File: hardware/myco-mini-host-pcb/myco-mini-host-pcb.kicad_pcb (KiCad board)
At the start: 2 copper layers, 190 x 115 mm, 22 parts, among them J1 Conn_01x17_Female, J2 Conn_01x17_Female, Q1 AO3401A, Q2 AO3401A, SW1 EM-04-Q, U1 XC9145B33C0R-G, U2 SHT40-AD1B-R2, U3 BH1750FVI-TR

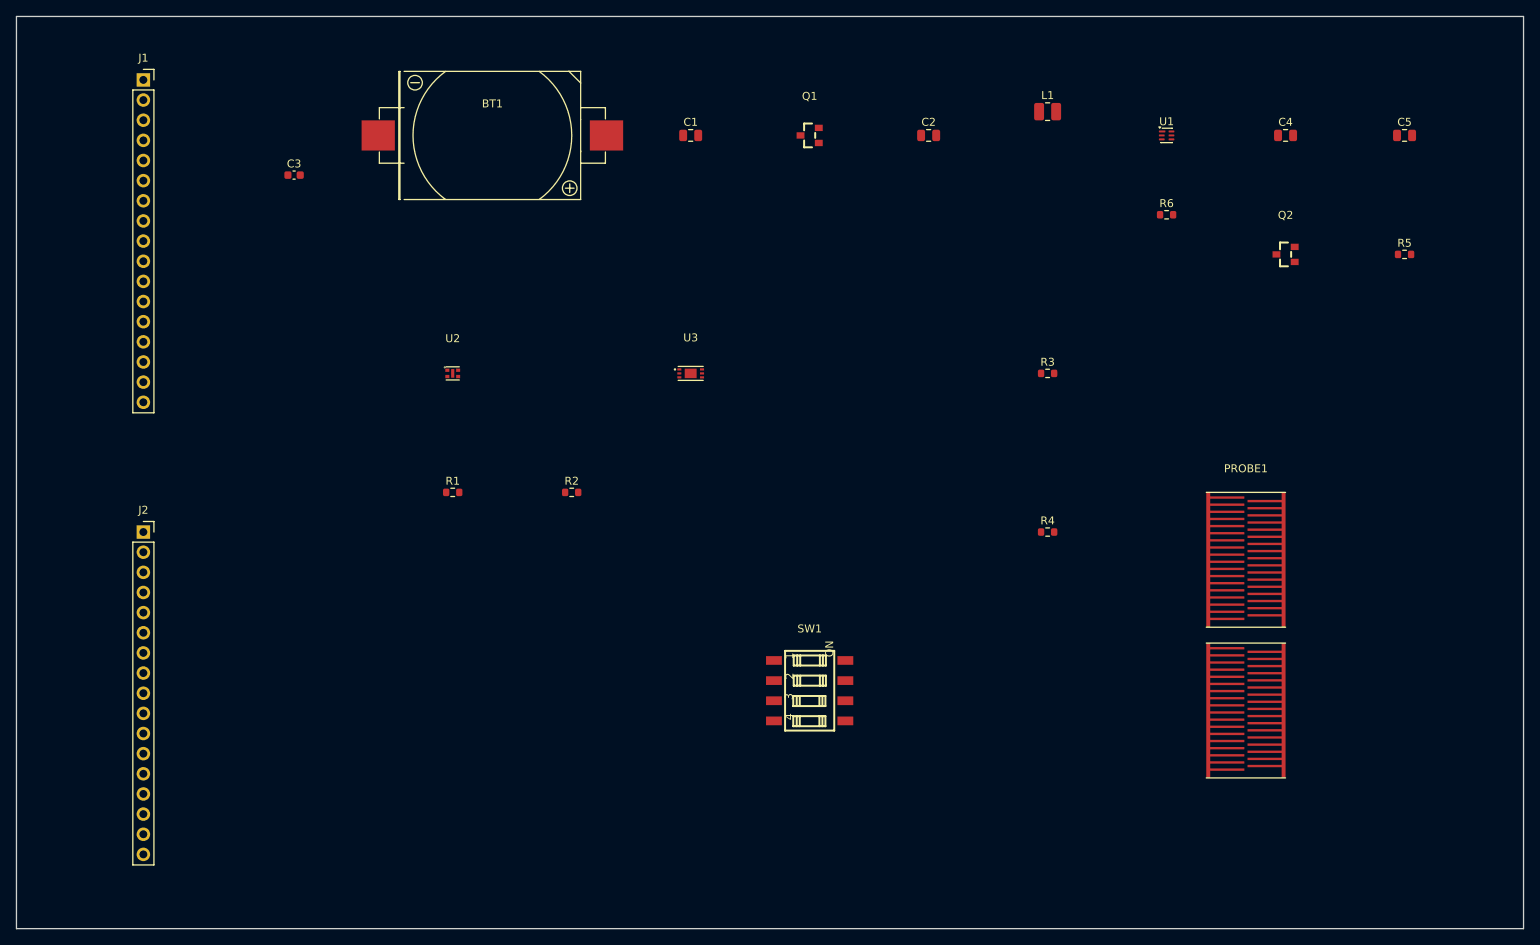
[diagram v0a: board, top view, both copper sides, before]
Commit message: fix: header rows J1/J2 en colonnes parallèles à 25.4mm (interface breakout réelle)
J1/J2 étaient empilés verticalement au lieu d'être côte à côte. Corrigé pour
matcher l'espacement centre-à-centre exact des headers J1/J4 du breakout
an54lq-15 (25.4mm, voir docs/host-pcb-design-brief.md sec.2).

Co-Authored-By: Claude Sonnet 5 <noreply@anthropic.com>
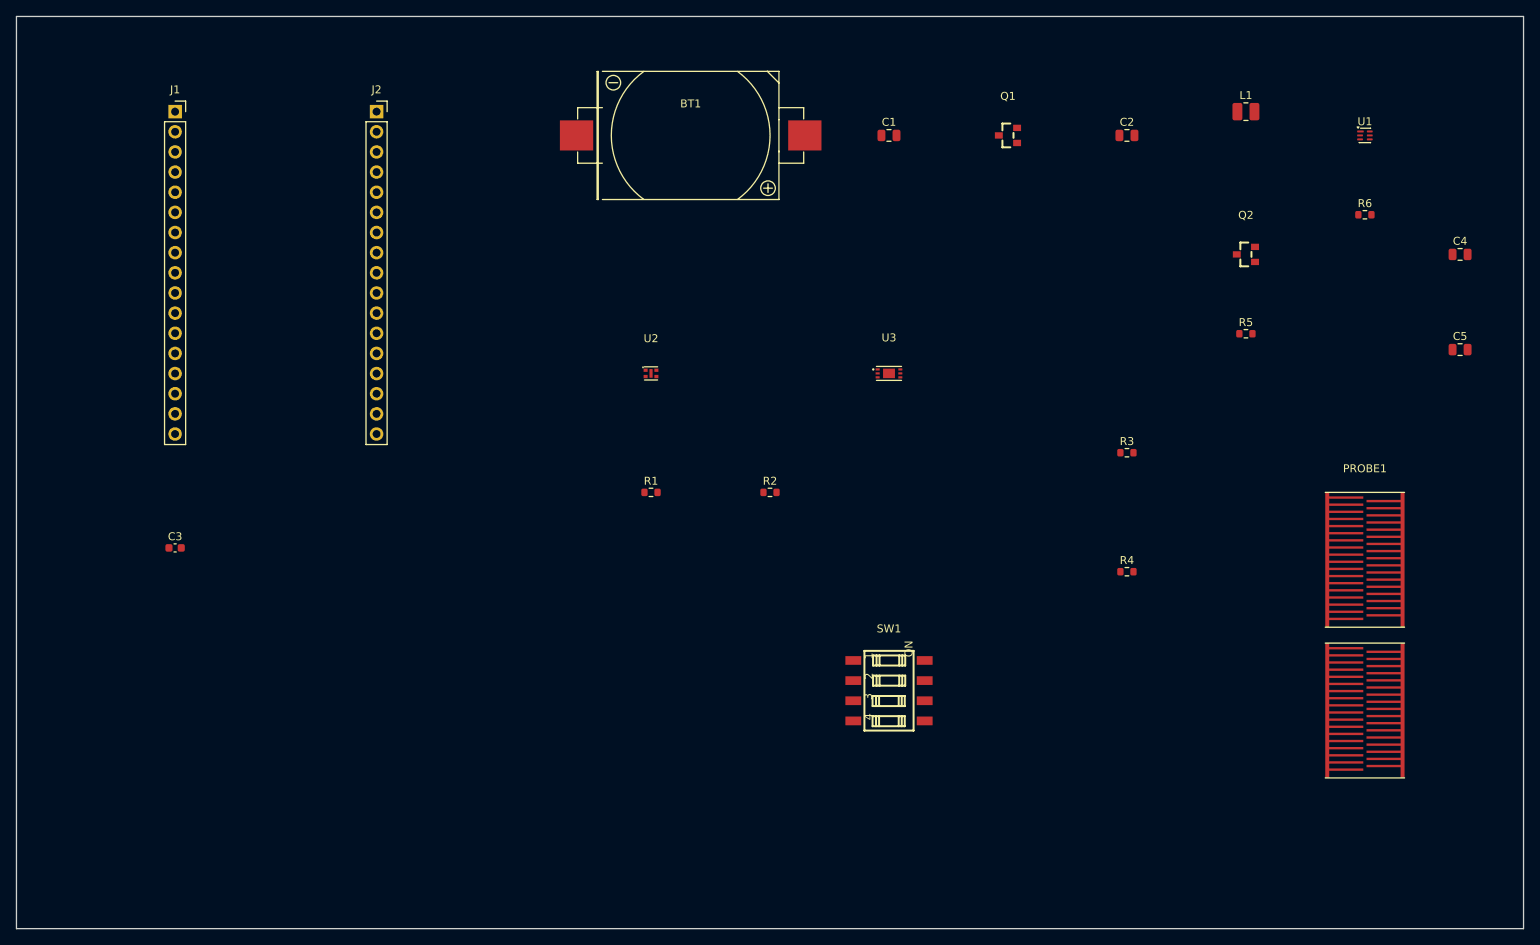
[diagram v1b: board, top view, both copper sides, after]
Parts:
- moved J2 60.6 mm to (45.4, 12.0)
- moved C3 49.3 mm to (20.0, 67.0)
- moved C5 27.9 mm to (182.0, 42.0)
- moved C4 26.6 mm to (182.0, 30.0)
- moved BT1 25.0 mm to (85.0, 15.0)
- moved C1 25.0 mm to (110.0, 15.0)
- moved C2 25.0 mm to (140.0, 15.0)
- moved L1 25.0 mm to (155.0, 12.0)
- moved Q1 25.0 mm to (125.0, 15.0)
- moved R1 25.0 mm to (80.0, 60.0)
- moved R2 25.0 mm to (95.0, 60.0)
- moved R6 25.0 mm to (170.0, 25.0)
- moved U1 25.0 mm to (170.0, 15.0)
- moved U2 25.0 mm to (80.0, 45.0)
- moved U3 25.0 mm to (110.0, 45.0)
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
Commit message: fix: DVI du BH1750 sur VDD_NRF au lieu de VOUT_3V3 (cohérence avec les pull-ups I2C)
Le datasheet ROHM BH1750FVI définit VIH1 = 0.7 x DVI comme seuil logique haut
sur SDA/SCL. DVI était câblée sur VOUT_3V3 (3.3V fixe) alors que les pull-ups
I2C (R1/R2) sont sur VDD_NRF (~3.0V CR2032, peut descendre vers ~2.0V en fin
de vie de pile) — le seuil (2.31V) pouvait dépasser la tension réelle du bus
en fin de vie de pile, empêchant le BH1750 de reconnaître un "haut" valide.
DVI câblée maintenant sur le même rail que les pull-ups pour que le seuil
suive la tension réelle du bus. Point de séquencement DVI/VCC résiduel
documenté dans docs/pcb-design-decisions.md (non tranché, à valider en test).

Co-Authored-By: Claude Sonnet 5 <noreply@anthropic.com>
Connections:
- U3 pad 5: VOUT_3V3 -> VDD_NRF
